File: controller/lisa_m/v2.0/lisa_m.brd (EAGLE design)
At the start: 50.7 x 33.6 mm, 119 parts, among them IC9 LP2992 5V, J1 CONN_3-1, J2 CONN_3-1, J3 CONN_3-1, J4 CONN_3-1, J5 CONN_3-1, J6 CONN_3-1, J7 CONN_3-1, J8 CONN_3-1, Q1 12Mhz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

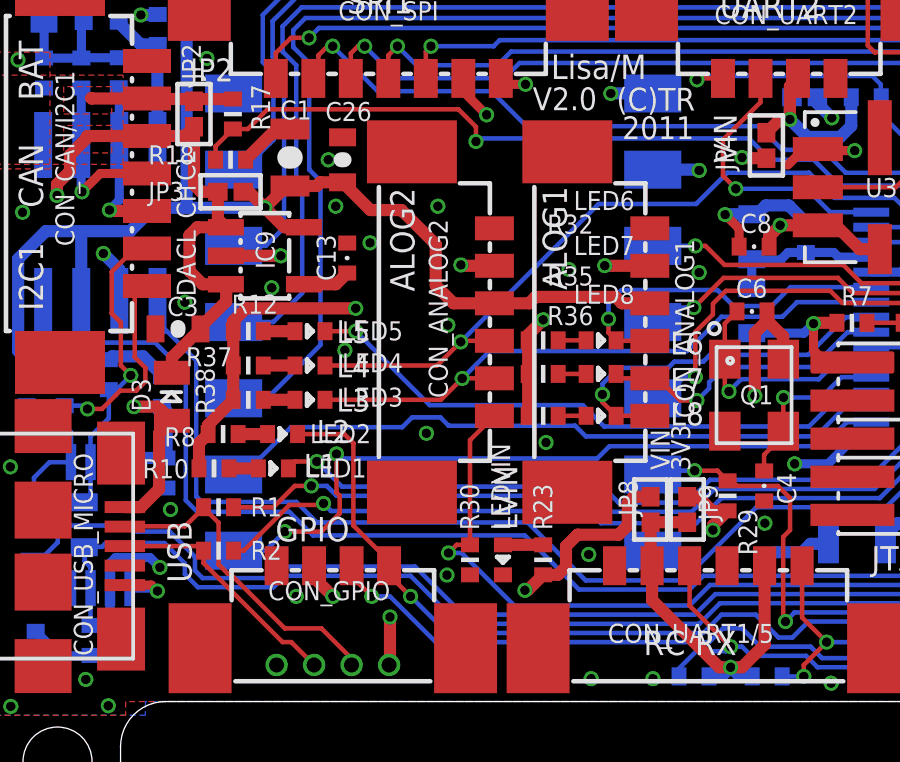
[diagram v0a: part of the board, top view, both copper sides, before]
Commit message: Updated led footprints to have placement information about orientation.
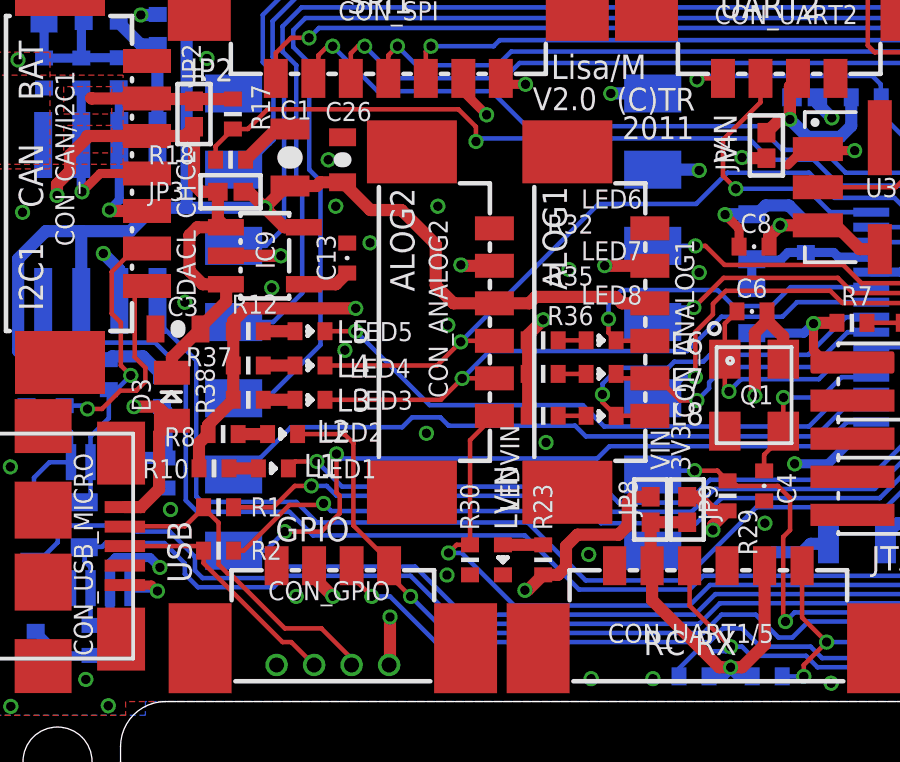
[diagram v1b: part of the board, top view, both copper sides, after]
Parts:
- turned LED1 to 180 degrees
- turned LED2 to 180 degrees
- turned LED3 to 180 degrees
- turned LED4 to 180 degrees
- turned LED5 to 180 degrees
- turned LED6 to 180 degrees
- turned LED7 to 180 degrees
- turned LED8 to 180 degrees
- turned LEDVIN to 90 degrees
